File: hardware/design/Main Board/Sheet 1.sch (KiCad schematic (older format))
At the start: 2 parts

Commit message: Version 1.0
Wrapped up design. Version for Detailed Design Review.
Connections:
- net Input Section/CH1+ renamed Bypass Relays/CH1_B-
- net Input Section/CH1- renamed Bypass Relays/CH1_B+
- net Input Section/CH2+ renamed Bypass Relays/CH2_B+
- net Input Section/CH2- renamed Bypass Relays/CH2_B-
- net Output Stage/CH1+_OUT renamed Bypass Relays/CH1+
- net Output Stage/CH1-_OUT renamed Bypass Relays/CH1-
- net Output Stage/CH2+_OUT renamed Bypass Relays/CH2+
- net Output Stage/CH2-_OUT renamed Bypass Relays/CH2-
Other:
- moved on the sheet: P?
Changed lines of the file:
@@
 EELAYER 27 0
 EELAYER END
-$Descr A4 11693 8268
+$Descr USLetter 11000 8500
 encoding utf-8
-Sheet 1 8
-Title ""
-Date "6 may 2014"
-Rev ""
-Comp ""
-Comment1 ""
+Sheet 1 9
+Title "Hybrid Audio Dynamics Processor"
+Date "10 may 2014"
+Rev "1.0"
+Comp "P14345"
+Comment1 "Top Level Schematic"
 Comment2 ""
 Comment3 ""
@@
 L CONN_4 P?
 U 1 1 534DB1BE
-P 1150 2600
-F 0 "P?" V 1100 2600 50  0000 C CNN
-F 1 "CONN_4" V 1200 2600 50  0000 C CNN
-F 2 "" H 1150 2600 60  0000 C CNN
-F 3 "" H 1150 2600 60  0000 C CNN
-	1    1150 2600
+P 700 2600
+F 0 "P?" V 650 2600 50  0000 C CNN
+F 1 "CONN_4" V 750 2600 50  0000 C CNN
+F 2 "" H 700 2600 60  0000 C CNN
+F 3 "" H 700 2600 60  0000 C CNN
+	1    700  2600
 	-1   0    0    -1
 $EndComp
@@
 F0 "Input Section" 50
 F1 "Sheet 2.sch" 50
-F2 "CH1-" I L 1700 2450 60
-F3 "CH1+" I L 1700 2550 60
+F2 "CH1-" I L 1700 2550 60
+F3 "CH1+" I L 1700 2450 60
 F4 "CH2+" I L 1700 2650 60
 F5 "CH2-" I L 1700 2750 60
@@
 $EndSheet
 Wire Wire Line
-	1500 2450 1700 2450
-Wire Wire Line
-	1500 2550 1700 2550
-Wire Wire Line
-	1500 2650 1700 2650
-Wire Wire Line
-	1500 2750 1700 2750
-$Sheet
-S 4450 4150 1650 700
+	1050 2650 1700 2650
+Wire Wire Line
+	1050 2750 1700 2750
+$Sheet
+S 4300 4900 1650 700
 U 534DCE54
 F0 "Precision Rectifier" 50
 F1 "Sheet 3.sch" 50
-F2 "CH1_RECT_IN" I L 4450 4350 60
-F3 "CH2_RECT_IN" I L 4450 4600 60
-F4 "CH1_RECT_OUT" O R 6100 4350 60
-F5 "CH2_RECT_OUT" O R 6100 4600 60
+F2 "CH1_RECT_IN" I L 4300 5100 60
+F3 "CH2_RECT_IN" I L 4300 5350 60
+F4 "CH1_RECT_OUT" O R 5950 5100 60
+F5 "CH2_RECT_OUT" O R 5950 5350 60
 $EndSheet
 Wire Wire Line
@@
 $EndSheet
 $Sheet
-S 6200 2250 1700 1200
+S 5750 2250 1700 1200
 U 534F2525
 F0 "Output Stage" 50
 F1 "Sheet 5.sch" 50
-F2 "CH1_LN_DVR_IN" I L 6200 2500 60
-F3 "CH1+_OUT" O R 7900 2500 60
-F4 "CH1-_OUT" O R 7900 2600 60
-F5 "CH2_LN_DVR_IN" I L 6200 2700 60
-F6 "CH2+_OUT" O R 7900 2700 60
-F7 "CH2-_OUT" O R 7900 2800 60
-$EndSheet
-Wire Wire Line
-	4800 2500 6200 2500
-Wire Wire Line
-	4800 2700 6200 2700
+F2 "CH1_LN_DVR_IN" I L 5750 2500 60
+F3 "CH1+_OUT" O R 7450 2500 60
+F4 "CH1-_OUT" O R 7450 2600 60
+F5 "CH2_LN_DVR_IN" I L 5750 2700 60
+F6 "CH2+_OUT" O R 7450 2700 60
+F7 "CH2-_OUT" O R 7450 2800 60
+$EndSheet
 $Comp
 L CONN_4 P?
 U 1 1 5362E417
-P 8950 2650
-F 0 "P?" V 8900 2650 50  0000 C CNN
-F 1 "CONN_4" V 9000 2650 50  0000 C CNN
-F 2 "" H 8950 2650 60  0000 C CNN
-F 3 "" H 8950 2650 60  0000 C CNN
-	1    8950 2650
+P 10250 2150
+F 0 "P?" V 10200 2150 50  0000 C CNN
+F 1 "CONN_4" V 10300 2150 50  0000 C CNN
+F 2 "" H 10250 2150 60  0000 C CNN
+F 3 "" H 10250 2150 60  0000 C CNN
+	1    10250 2150
 	1    0    0    -1
 $EndComp
 $Sheet
-S 3050 4150 1150 700
+S 2900 4900 1150 700
 U 5362F285
 F0 "LPF" 50
 F1 "Sheet 6.sch" 50
-F2 "LPF_IN_1" I L 3050 4350 60
-F3 "LPF_IN_2" I L 3050 4600 60
-F4 "LPF_OUT_1" O R 4200 4350 60
-F5 "LPF_OUT_2" O R 4200 4600 60
-$EndSheet
-Wire Wire Line
-	3050 4350 2750 4350
-Wire Wire Line
-	2750 4350 2750 2500
+F2 "LPF_IN_1" I L 2900 5100 60
+F3 "LPF_IN_2" I L 2900 5350 60
+F4 "LPF_OUT_1" O R 4050 5100 60
+F5 "LPF_OUT_2" O R 4050 5350 60
+$EndSheet
+Wire Wire Line
+	2750 2500 2750 5100
 Connection ~ 2750 2500
 Wire Wire Line
-	2650 2700 2650 4600
-Wire Wire Line
-	2650 4600 3050 4600
+	2650 2700 2650 5350
 Connection ~ 2650 2700
 Wire Wire Line
-	4200 4350 4450 4350
-Wire Wire Line
-	4200 4600 4450 4600
-Wire Wire Line
-	8600 2500 7900 2500
-Wire Wire Line
-	8600 2600 7900 2600
-Wire Wire Line
-	8600 2700 7900 2700
-Wire Wire Line
-	8600 2800 7900 2800
-$Sheet
-S 6800 4100 1550 1350
+	4050 5100 4300 5100
+Wire Wire Line
+	4050 5350 4300 5350
+$Sheet
+S 6300 4250 1550 1350
 U 53665ABB
 F0 "MCU" 50
 F1 "Sheet 7.sch" 50
-$EndSheet
+F2 "A_IN_1" I L 6300 5100 60
+F3 "A_IN_2" I L 6300 5350 60
+F4 "RELAY_1" O R 7850 4450 60
+F5 "RELAY_2" O R 7850 4550 60
+F6 "CH1_CV" O L 6300 4450 60
+F7 "CH2_CV" O L 6300 4650 60
+F8 "CH1_MUG" O L 6300 4350 60
+F9 "CH2_MUG" O L 6300 4550 60
+$EndSheet
+Wire Wire Line
+	2750 5100 2900 5100
+Wire Wire Line
+	2650 5350 2900 5350
+Wire Wire Line
+	5950 5100 6300 5100
+Wire Wire Line
+	5950 5350 6300 5350
+Wire Wire Line
+	6300 4350 5650 4350
+Wire Wire Line
+	5650 4350 5650 2900
+Wire Wire Line
+	5650 2900 4800 2900
+Wire Wire Line
+	6300 4450 5600 4450
+Wire Wire Line
+	5600 4450 5600 3000
+Wire Wire Line
+	5600 3000 4800 3000
+Wire Wire Line
+	6300 4550 5550 4550
+Wire Wire Line
+	5550 4550 5550 3100
+Wire Wire Line
+	5550 3100 4800 3100
+Wire Wire Line
+	6300 4650 5500 4650
+Wire Wire Line
+	5500 4650 5500 3200
+Wire Wire Line
+	5500 3200 4800 3200
+$Sheet
+S 7900 1400 1150 1800
+U 536F9075
+F0 "Bypass Relays" 50
+F1 "Sheet 8.sch" 50
+F2 "RELAY_1" I R 9050 2800 60
+F3 "RELAY_2" I R 9050 2700 60
+F4 "CH1_A+" I L 7900 2500 60
+F5 "CH1_B+" I L 7900 1700 60
+F6 "CH1_A-" I L 7900 2600 60
+F7 "CH1_B-" I L 7900 1800 60
+F8 "CH1+" O R 9050 2000 60
+F9 "CH1-" O R 9050 2100 60
+F10 "CH2_A+" I L 7900 2700 60
+F11 "CH2_B+" I L 7900 1900 60
+F12 "CH2_A-" I L 7900 2800 60
+F13 "CH2_B-" I L 7900 2000 60
+F14 "CH2+" O R 9050 2200 60
+F15 "CH2-" O R 9050 2300 60
+$EndSheet
+Wire Wire Line
+	1050 2450 1700 2450
+Wire Wire Line
+	1050 2550 1700 2550
+Wire Wire Line
+	7900 1700 1150 1700
+Wire Wire Line
+	1150 1700 1150 2450
+Connection ~ 1150 2450
+Wire Wire Line
+	7900 1800 1250 1800
+Wire Wire Line
+	1250 1800 1250 2550
+Connection ~ 1250 2550
+Wire Wire Line
+	7900 1900 1350 1900
+Wire Wire Line
+	1350 1900 1350 2650
+Connection ~ 1350 2650
+Wire Wire Line
+	7900 2000 1450 2000
+Wire Wire Line
+	1450 2000 1450 2750
+Connection ~ 1450 2750
+Wire Wire Line
+	7450 2800 7900 2800
+Wire Wire Line
+	7450 2700 7900 2700
+Wire Wire Line
+	7450 2600 7900 2600
+Wire Wire Line
+	7450 2500 7900 2500
+Wire Wire Line
+	7850 4450 9200 4450
+Wire Wire Line
+	9200 4450 9200 2800
+Wire Wire Line
+	9200 2800 9050 2800
+Wire Wire Line
+	9050 2700 9300 2700
+Wire Wire Line
+	9300 2700 9300 4550
+Wire Wire Line
+	9300 4550 7850 4550
+Wire Wire Line
+	9050 2000 9900 2000
+Wire Wire Line
+	9050 2100 9900 2100
+Wire Wire Line
+	9050 2200 9900 2200
+Wire Wire Line
+	9050 2300 9900 2300
+Wire Wire Line
+	4800 2500 5750 2500
+Wire Wire Line
+	4800 2700 5750 2700
 $EndSCHEMATC

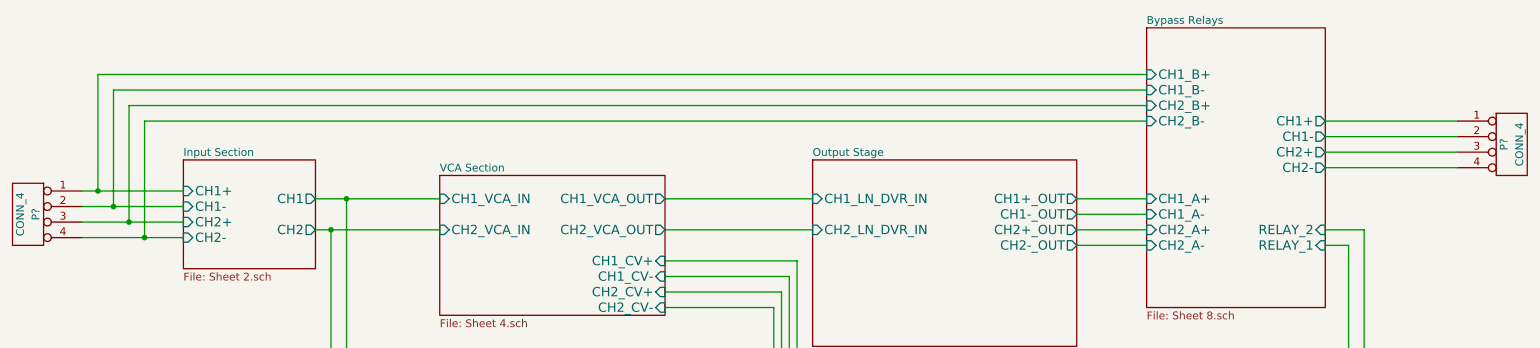
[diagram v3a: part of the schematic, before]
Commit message: Version 1.0.082514.2134
Initial partial PCB layout.
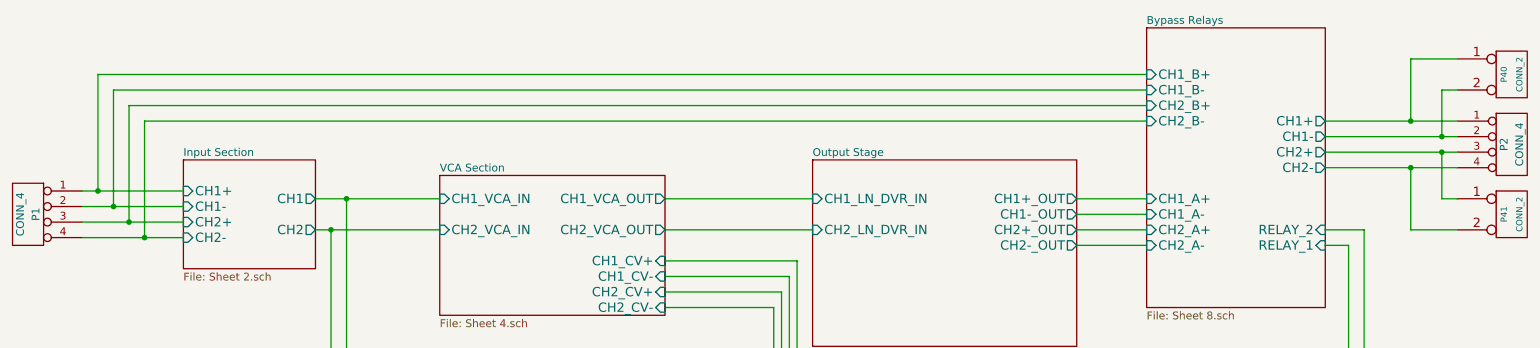
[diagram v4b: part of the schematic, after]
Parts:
- added P40, P41: CONN_2, symbol CONN_2
- gave numbers to parts that had none: 2
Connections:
- net Bypass Relays/CH1+: now also P40.1 (P1)
- net Bypass Relays/CH1-: now also P40.2 (PM)
- net Bypass Relays/CH2+: now also P41.1 (P1)
- net Bypass Relays/CH2-: now also P41.2 (PM)
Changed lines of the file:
@@
 Sheet 1 9
 Title "Hybrid Audio Dynamics Processor"
-Date "15 may 2014"
+Date "26 aug 2014"
 Rev "1.0"
 Comp "P14345"
@@
 $EndDescr
 $Comp
-L CONN_4 P?
+L CONN_4 P1
 U 1 1 534DB1BE
 P 700 2600
-F 0 "P?" V 650 2600 50  0000 C CNN
+F 0 "P1" V 650 2600 50  0000 C CNN
 F 1 "CONN_4" V 750 2600 50  0000 C CNN
 F 2 "" H 700 2600 60  0000 C CNN
@@
 $EndSheet
 $Comp
-L CONN_4 P?
+L CONN_4 P2
 U 1 1 5362E417
 P 10250 2150
-F 0 "P?" V 10200 2150 50  0000 C CNN
+F 0 "P2" V 10200 2150 50  0000 C CNN
 F 1 "CONN_4" V 10300 2150 50  0000 C CNN
 F 2 "" H 10250 2150 60  0000 C CNN
@@
 Wire Wire Line
 	4800 2700 5750 2700
+$Comp
+L CONN_2 P40
+U 1 1 53FBDF54
+P 10250 1700
+F 0 "P40" V 10200 1700 40  0000 C CNN
+F 1 "CONN_2" V 10300 1700 40  0000 C CNN
+F 2 "" H 10250 1700 60  0000 C CNN
+F 3 "" H 10250 1700 60  0000 C CNN
+	1    10250 1700
+	1    0    0    -1
+$EndComp
+$Comp
+L CONN_2 P41
+U 1 1 53FBE125
+P 10250 2600
+F 0 "P41" V 10200 2600 40  0000 C CNN
+F 1 "CONN_2" V 10300 2600 40  0000 C CNN
+F 2 "" H 10250 2600 60  0000 C CNN
+F 3 "" H 10250 2600 60  0000 C CNN
+	1    10250 2600
+	1    0    0    -1
+$EndComp
+Wire Wire Line
+	9900 1800 9800 1800
+Wire Wire Line
+	9800 1800 9800 2100
+Connection ~ 9800 2100
+Wire Wire Line
+	9900 1600 9600 1600
+Wire Wire Line
+	9600 1600 9600 2000
+Connection ~ 9600 2000
+Wire Wire Line
+	9900 2500 9800 2500
+Wire Wire Line
+	9800 2500 9800 2200
+Connection ~ 9800 2200
+Wire Wire Line
+	9900 2700 9600 2700
+Wire Wire Line
+	9600 2700 9600 2300
+Connection ~ 9600 2300
 $EndSCHEMATC

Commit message: Version 1.0.090114.2238
Completed Layout
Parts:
- added P100, P101, P102, P103, P104, P105, P106, P107, P108, P109, P110, P111: TST, ~, symbol TST
- added P200: CONN_5, symbol CONN_5
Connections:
- new net +3.3V: P106.1, P107.1, P200.5
- new net +5V: P108.1, P109.1, P200.4
- new net GND: P100.1, P101.1, P102.1, P103.1, P200.1
- new net VDD: P110.1, P111.1, P200.2
- new net VSS: P104.1, P105.1, P200.3
